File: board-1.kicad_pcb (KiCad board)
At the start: 2 copper layers, 52.7 x 38.1 mm, 20 parts, among them P1 RESET, P2 USB, P3 CONN_01X07, P4 CONN_01X05, P5 CONN_01X02, U1 MCP1700, U2 PIC32MX2XX, Y1 24MHz

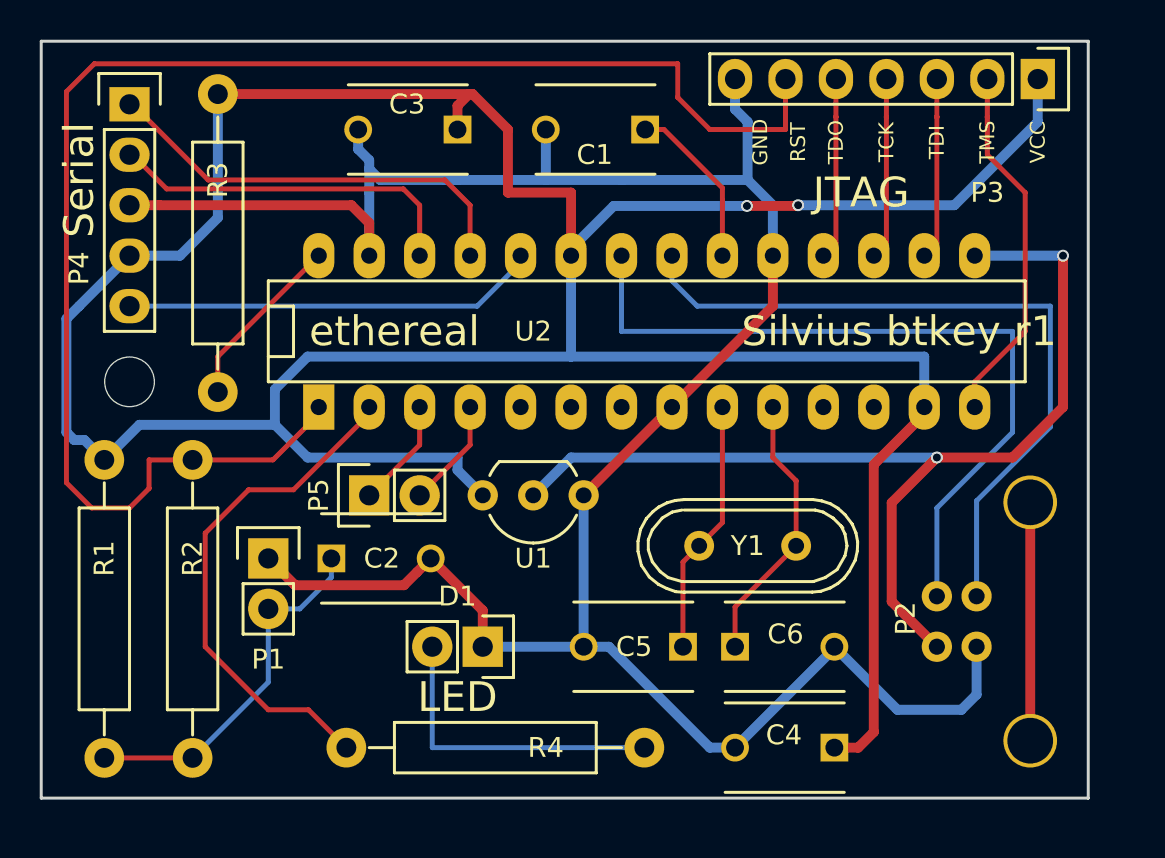
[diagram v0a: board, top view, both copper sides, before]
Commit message: Added diode between USB power in and voltage regulator.
Also added OSHW logo.
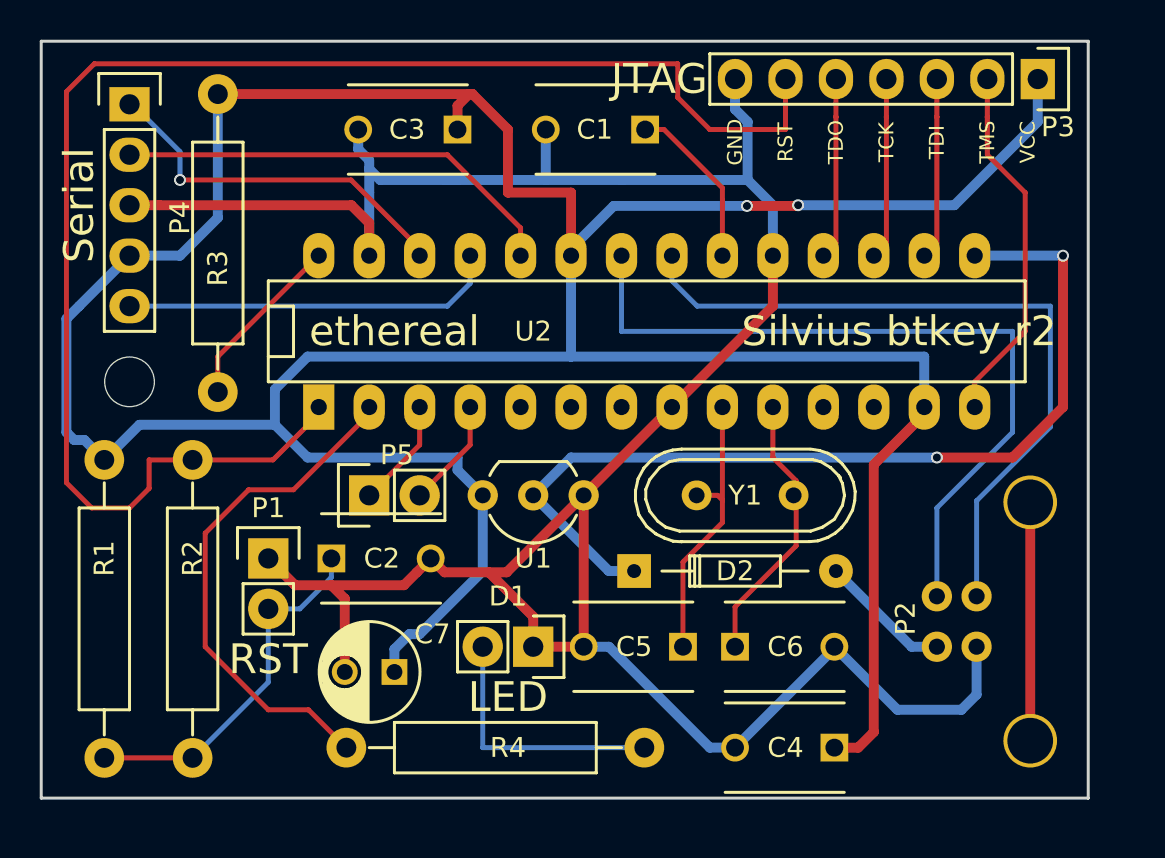
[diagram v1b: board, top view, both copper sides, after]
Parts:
- added C7: 47uF, Capacitors_ThroughHole:C_Radial_D5_L6_P2.5, F.Cu at (142.9, 72.4)
- added D2: D, Diodes_ThroughHole:Diode_DO-35_SOD27_Horizontal_RM10, F.Cu at (154.9, 67.3)
- added oshw: , footprint:oshw-small-2, B.Cu at (134.6, 63.5)
- moved Y1 2.54 mm to (160.5, 63.5)
- moved D1 2.54 mm to (149.9, 71.1)
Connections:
- P2 pad 1: Net-(P2-Pad1) -> Net-(D2-Pad2)
- P5 pad 1: /UART_SND -> /UART_RCV
- P5 pad 2: /UART_RCV -> /UART_SND
- U1 pad 2: Net-(P2-Pad1) -> Net-(D2-Pad1)
- U2 pad 15: Net-(P2-Pad1) -> Net-(D2-Pad1)
- U2 pad 24: Net-(P4-Pad5) -> Net-(P4-Pad2)
- U2 pad 25: Net-(P4-Pad1) -> Net-(P4-Pad5)
- U2 pad 26: Net-(P4-Pad2) -> Net-(P4-Pad1)
- U2 pad 3: /UART_SND -> /UART_RCV
- U2 pad 4: /UART_RCV -> /UART_SND
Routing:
- net Net-(P2-Pad1): track 52.0 -> 0.00 mm, vias 2 -> 0
- net Net-(D2-Pad1): track 0.00 -> 47.2 mm, vias 0 -> 2
- net +3V3: track 163.6 -> 174.6 mm
- net GND: track 125.3 -> 136.1 mm
- net Net-(D2-Pad2): track 0.00 -> 6.66 mm
- net Net-(P4-Pad2): track 18.2 -> 23.1 mm
- net Net-(P4-Pad1): track 21.8 -> 19.0 mm, vias 0 -> 1
- net Net-(D1-Pad2): track 15.8 -> 13.2 mm
- net Net-(P4-Pad5): track 20.9 -> 19.0 mm
- net Net-(C5-Pad1): track 12.9 -> 14.3 mm
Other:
- board text added: "3V3"
- board text added: "AT"
- board text added: "Silvius btkey r2"
- board text added: "Silvius project by dwk@voxhub.io Hardware r1-2 by ethereal@ethv.net"
- board text added: "μRX"
- board text added: "μTX"
- board text removed: "Silvius btkey r1"
- board text removed: "Silvius project by dwk@voxhub.io Hardware r1 by ethereal@ethv.net"

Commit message: Made more compliant with OHL requirements.
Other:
- board text added: "Licensed under CERN OHL v.1.2"
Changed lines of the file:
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@@
     (area 120.854536 37.236666 179.535 79.125001)
     (thickness 1.6)
-    (drawings 27)
+    (drawings 28)
     (tracks 224)
     (zones 0)
@@
     )
   )
+  (gr_text "Licensed under CERN OHL v.1.2" (at 150.368 48.768) (layer B.SilkS)
+    (effects (font (size 0.75 0.75) (thickness 0.1875)) (justify mirror))
+  )
   (gr_text RST (at 136.525 71.755) (layer F.SilkS)

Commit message: Revision 3.
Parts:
- P1: value RESET -> CONN_01X03; footprint Pin_Headers:Pin_Header_Straight_1x02 -> Pin_Headers:Pin_Header_Straight_1x03
- P2: value USB -> USB_B_fixed
- R1, R2, R4: footprint Resistors_ThroughHole:Resistor_Horizontal_RM15mm -> Resistors_ThroughHole:Resistor_Horizontal_RM10mm
- moved P1 6.68 mm to (143.2, 66.8), turned to 90 degrees
- moved C2 4.30 mm to (135.4, 66.7)
- moved oshw 2.11 mm to (134.4, 65.6)
- moved U1 0.95 mm to (153.3, 63.6)
- moved P5 0.94 mm to (140.7, 63.5)
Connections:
- P1 pad 1: GND -> Net-(P1-Pad1)
- P1 pad 2: Net-(C2-Pad1) -> Net-(P1-Pad2)
- P2 pad 1: Net-(D2-Pad2) -> /USB_N
- P2 pad 2: /USB_DN -> Net-(D2-Pad2)
- P2 pad 3: /USB_DP -> GND
- P2 pad 4: GND -> /USB_P
- U2 pad 21: /USB_DP -> /USB_P
- U2 pad 22: /USB_DN -> /USB_N
- U2 pad 5: Net-(U2-Pad5) -> Net-(P1-Pad1)
- U2 pad 6: Net-(U2-Pad6) -> Net-(P1-Pad2)
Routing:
- net /USB_N: track 0.00 -> 41.8 mm, vias 0 -> 1
- net /USB_P: track 0.00 -> 41.0 mm, vias 0 -> 1
- net /USB_DN: track 38.4 -> 0.00 mm
- net /USB_DP: track 37.0 -> 0.00 mm
- net Net-(P1-Pad2): track 0.00 -> 11.0 mm
- net Net-(P1-Pad1): track 0.00 -> 10.2 mm
- net GND: track 136.1 -> 128.1 mm
- net +3V3: track 174.6 -> 181.1 mm
- net Net-(C2-Pad1): track 18.3 -> 13.2 mm
- net Net-(D1-Pad2): track 13.2 -> 10.8 mm
- net /StatusLED: track 26.0 -> 28.4 mm
- net /UART_RCV: track 5.50 -> 7.18 mm
- net Net-(D2-Pad2): track 6.66 -> 5.61 mm
- net /UART_SND: track 5.50 -> 6.44 mm
- net Net-(D2-Pad1): track 47.2 -> 46.6 mm
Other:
- board text added: "IO0"
- board text added: "IO1"
- board text added: "Silvius btkey r3"
- board text added: "Silvius project by dwk@voxhub.io Hardware r1-3 by ethereal@ethv.net"
- board text removed: "Silvius btkey r2"
- board text removed: "Silvius project by dwk@voxhub.io Hardware r1-2 by ethereal@ethv.net"

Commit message: Updated capacitor footprints.
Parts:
- C1, C2, C3, C4, C5, C6: footprint Capacitors_ThroughHole:C_Disc_D6_P5 -> Capacitors_ThroughHole:C_Rect_L7_W2.5_P5
